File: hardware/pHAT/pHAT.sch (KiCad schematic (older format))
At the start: 16 parts, among them P1 Conn_02x20_Odd_Even, U2 HIH6131-021, U3 P82B96

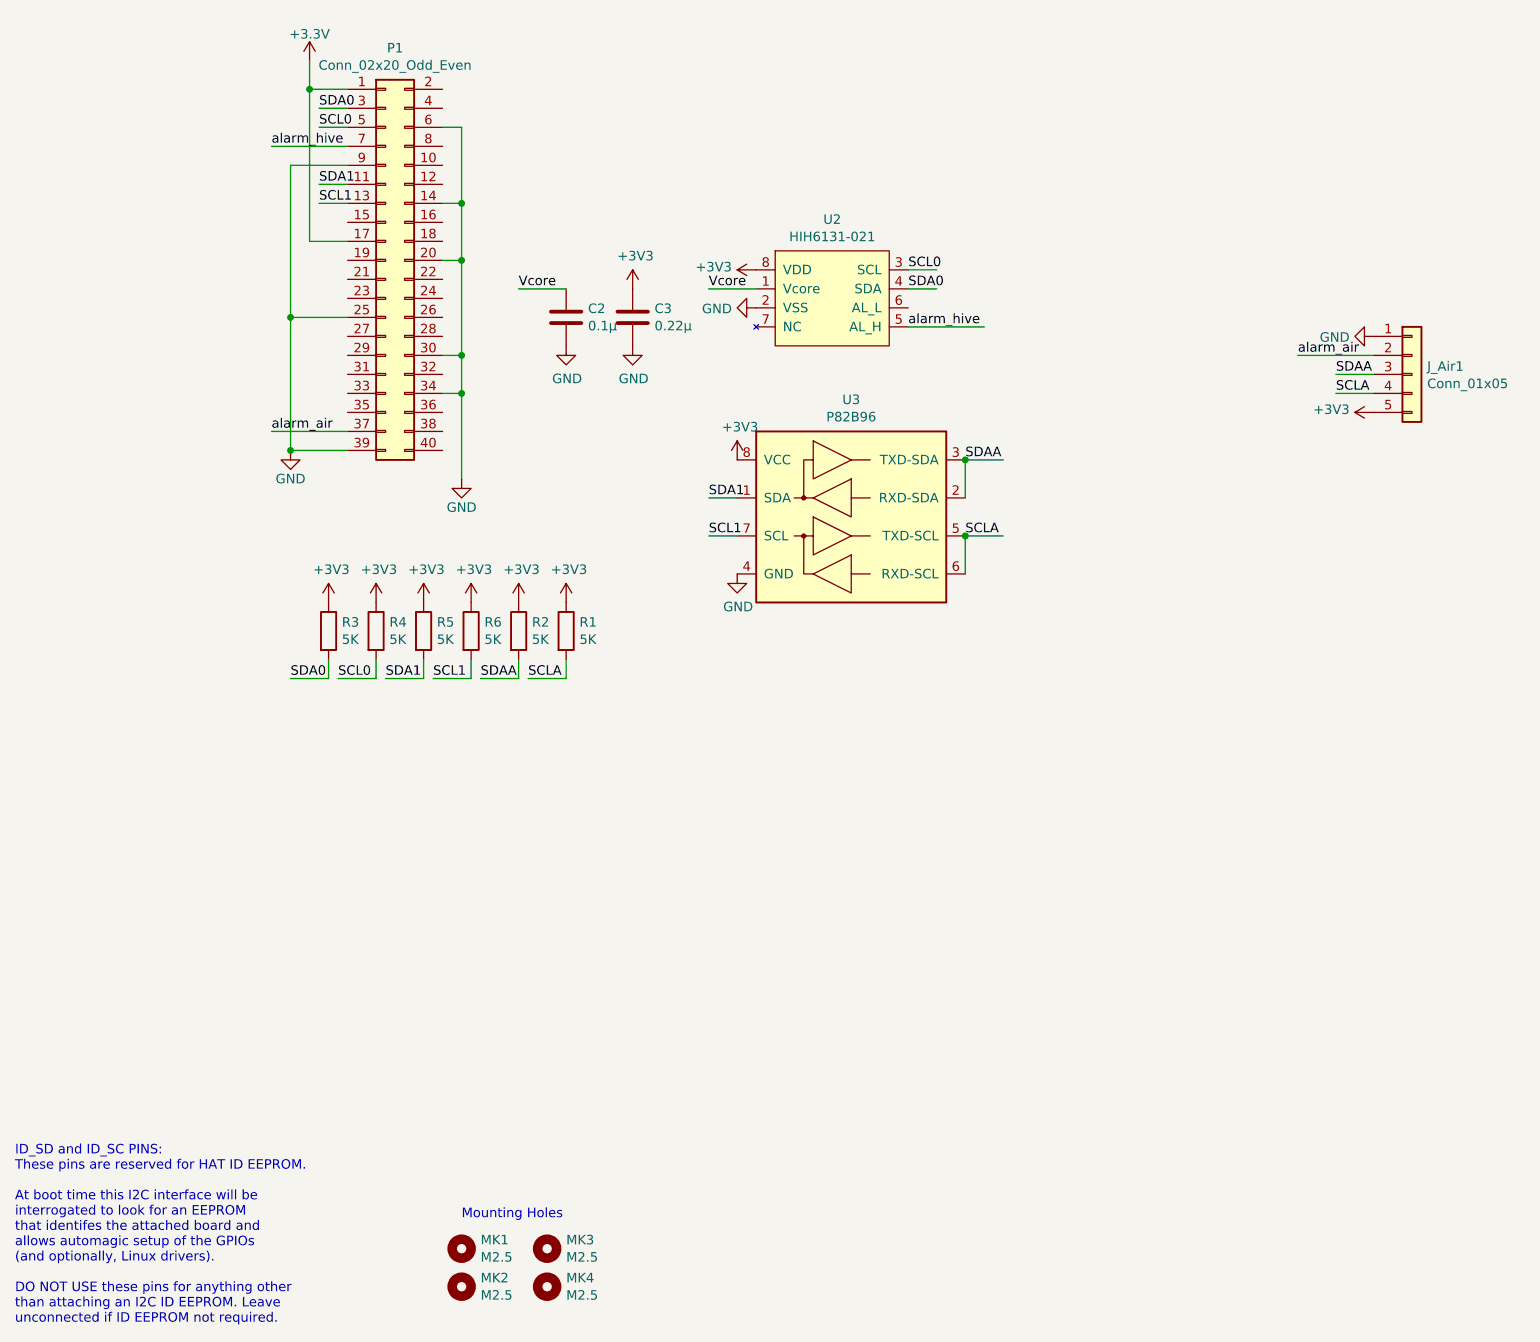
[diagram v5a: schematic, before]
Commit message: Preparing layout for adding a fan
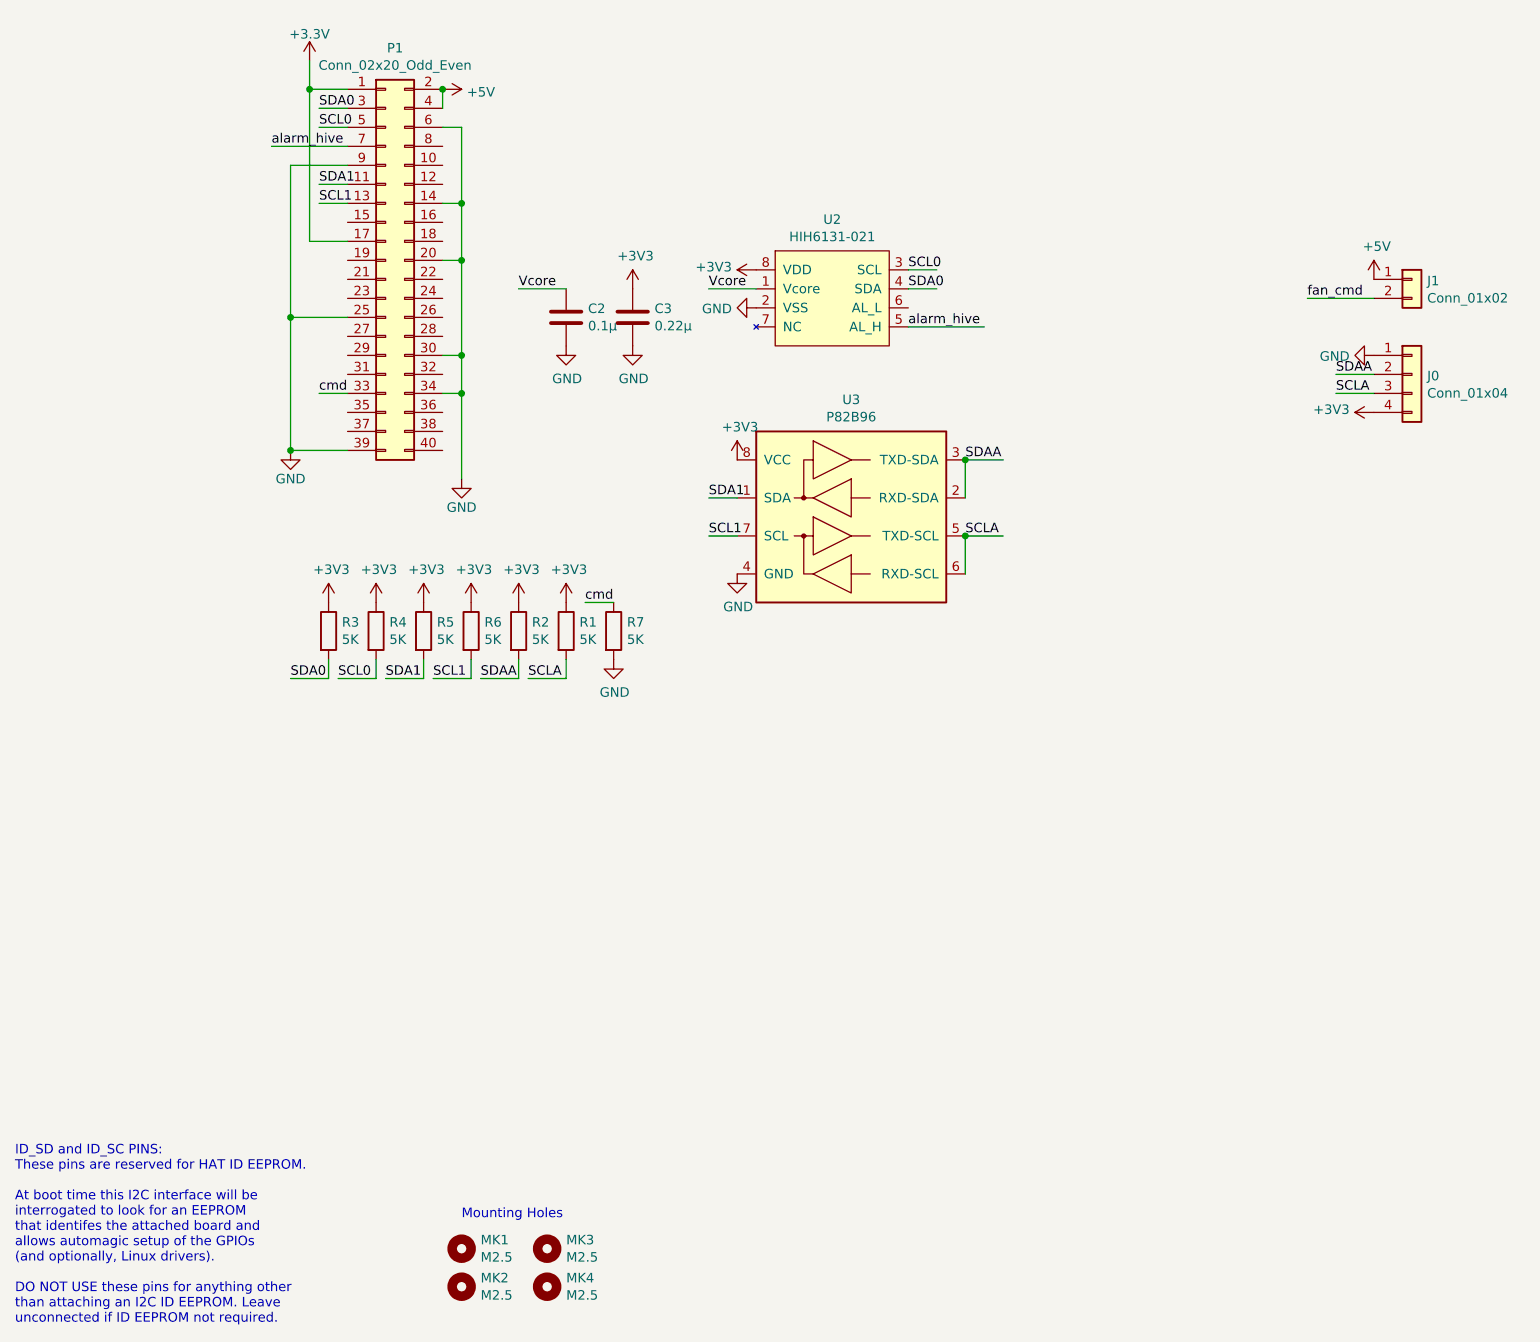
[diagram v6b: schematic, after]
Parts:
- removed J_Air1: Conn_01x05, Connector_Molex:Molex_KK-254_AE-6410-05A_1x05_P2.54mm_Vertical, symbol Connector_Generic:Conn_01x05
- added J0: Conn_01x04, Connector_Molex:Molex_KK-254_AE-6410-04A_1x04_P2.54mm_Vertical, symbol Connector_Generic:Conn_01x04
- added J1: Conn_01x02, Connector_Molex:Molex_KK-254_AE-6410-02A_1x02_P2.54mm_Vertical, symbol Connector_Generic:Conn_01x02
- added R7: 5K, Resistor_SMD:R_0805_2012Metric_Pad1.15x1.40mm_HandSolder, symbol Device:R
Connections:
- net labels added: +5V, cmd, fan_cmd
- net labels removed: alarm_air
- wire segments 51 -> 53
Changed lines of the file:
@@
 Sheet 1 1
 Title "Beehive pHAT"
-Date "2019-01-29"
-Rev "v2.1"
+Date "2019-02-13"
+Rev "v3.2"
 Comp "University of Glasgow"
 Comment1 ""
@@
 L power:GND #PWR0121
 U 1 1 5C4780F6
-P 7800 2400
-F 0 "#PWR0121" H 7800 2150 50  0001 C CNN
-F 1 "GND" V 7805 2272 50  0000 R CNN
-F 2 "" H 7800 2400 50  0001 C CNN
-F 3 "" H 7800 2400 50  0001 C CNN
-	1    7800 2400
+P 7800 2500
+F 0 "#PWR0121" H 7800 2250 50  0001 C CNN
+F 1 "GND" V 7805 2372 50  0000 R CNN
+F 2 "" H 7800 2500 50  0001 C CNN
+F 3 "" H 7800 2500 50  0001 C CNN
+	1    7800 2500
 	0    1    1    0
 $EndComp
@@
 	1    0    0    -1
 $EndComp
-$Comp
-L Connector_Generic:Conn_01x05 J_Air1
-U 1 1 5C50B707
-P 8000 2600
-F 0 "J_Air1" H 8080 2642 50  0000 L CNN
-F 1 "Conn_01x05" H 8080 2551 50  0000 L CNN
-F 2 "Connector_Molex:Molex_KK-254_AE-6410-05A_1x05_P2.54mm_Vertical" H 8000 2600 50  0001 C CNN
-F 3 "~" H 8000 2600 50  0001 C CNN
-	1    8000 2600
-	1    0    0    -1
-$EndComp
-Text Label 7400 2500 0    50   ~ 0
-alarm_air
-Wire Wire Line
-	7800 2500 7400 2500
 Text Label 2000 1400 0    50   ~ 0
 alarm_hive
 Wire Wire Line
 	2400 1400 2000 1400
-Text Label 2000 2900 0    50   ~ 0
-alarm_air
-Wire Wire Line
-	2400 2900 2000 2900
 $Comp
 L honeywell:HIHxx3x-021 U2
@@
 Wire Wire Line
 	3550 2150 3300 2150
+$Comp
+L Connector_Generic:Conn_01x04 J0
+U 1 1 5C646ECB
+P 8000 2600
+F 0 "J0" H 8080 2592 50  0000 L CNN
+F 1 "Conn_01x04" H 8080 2501 50  0000 L CNN
+F 2 "Connector_Molex:Molex_KK-254_AE-6410-04A_1x04_P2.54mm_Vertical" H 8000 2600 50  0001 C CNN
+F 3 "~" H 8000 2600 50  0001 C CNN
+	1    8000 2600
+	1    0    0    -1
+$EndComp
+$Comp
+L Connector_Generic:Conn_01x02 J1
+U 1 1 5C648B5C
+P 8000 2100
+F 0 "J1" H 8080 2092 50  0000 L CNN
+F 1 "Conn_01x02" H 8080 2001 50  0000 L CNN
+F 2 "Connector_Molex:Molex_KK-254_AE-6410-02A_1x02_P2.54mm_Vertical" H 8000 2100 50  0001 C CNN
+F 3 "~" H 8000 2100 50  0001 C CNN
+	1    8000 2100
+	1    0    0    -1
+$EndComp
+$Comp
+L power:+5V #PWR0101
+U 1 1 5C648C36
+P 7800 2100
+F 0 "#PWR0101" H 7800 1950 50  0001 C CNN
+F 1 "+5V" H 7815 2273 50  0000 C CNN
+F 2 "" H 7800 2100 50  0001 C CNN
+F 3 "" H 7800 2100 50  0001 C CNN
+	1    7800 2100
+	1    0    0    -1
+$EndComp
+$Comp
+L power:+5V #PWR0102
+U 1 1 5C648D8A
+P 2900 1100
+F 0 "#PWR0102" H 2900 950 50  0001 C CNN
+F 1 "+5V" V 2915 1228 50  0000 L CNN
+F 2 "" H 2900 1100 50  0001 C CNN
+F 3 "" H 2900 1100 50  0001 C CNN
+	1    2900 1100
+	0    1    1    0
+$EndComp
+Wire Wire Line
+	2900 1200 2900 1100
+Connection ~ 2900 1100
+Text Label 7450 2200 0    50   ~ 0
+fan_cmd
+Wire Wire Line
+	7800 2200 7450 2200
+Text Label 2250 2700 0    50   ~ 0
+cmd
+Wire Wire Line
+	2400 2700 2250 2700
+$Comp
+L Device:R R7
+U 1 1 5C66B531
+P 3800 3950
+F 0 "R7" H 3870 3996 50  0000 L CNN
+F 1 "5K" H 3870 3905 50  0000 L CNN
+F 2 "Resistor_SMD:R_0805_2012Metric_Pad1.15x1.40mm_HandSolder" V 3730 3950 50  0001 C CNN
+F 3 "~" H 3800 3950 50  0001 C CNN
+	1    3800 3950
+	1    0    0    -1
+$EndComp
+Text Label 3650 3800 0    50   ~ 0
+cmd
+Wire Wire Line
+	3800 3800 3650 3800
+$Comp
+L power:GND #PWR?
+U 1 1 5C6704A6
+P 3800 4100
+F 0 "#PWR?" H 3800 3850 50  0001 C CNN
+F 1 "GND" H 3805 3927 50  0000 C CNN
+F 2 "" H 3800 4100 50  0001 C CNN
+F 3 "" H 3800 4100 50  0001 C CNN
+	1    3800 4100
+	1    0    0    -1
+$EndComp
 $EndSCHEMATC

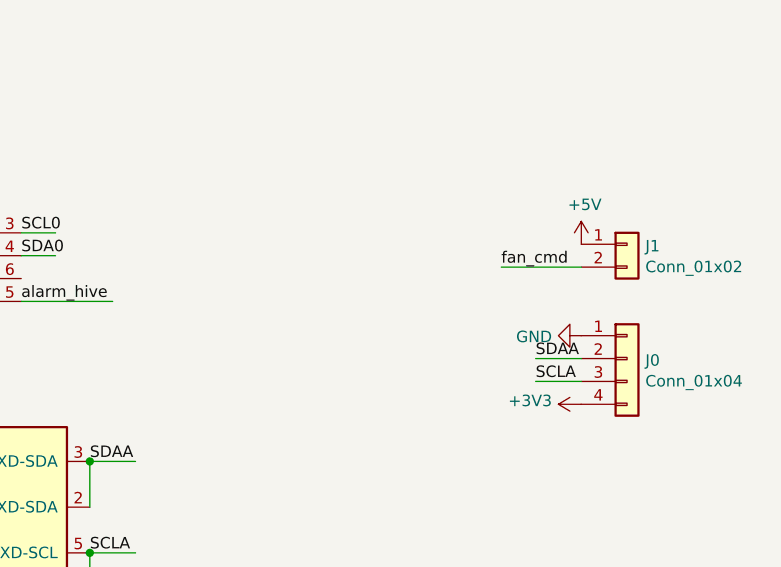
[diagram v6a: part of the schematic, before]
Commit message: Finished fan command circuit (pHAT v3.2)
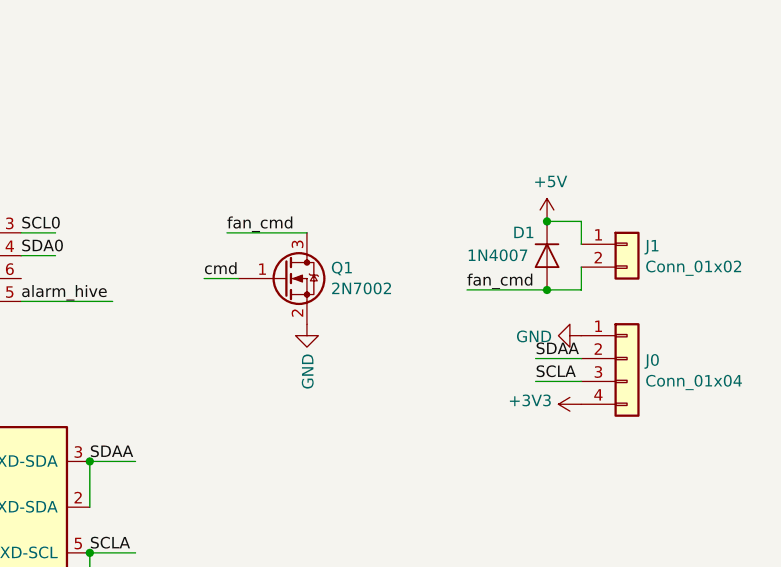
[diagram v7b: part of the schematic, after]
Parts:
- added D1: 1N4007, Diode_THT:D_DO-41_SOD81_P10.16mm_Horizontal, symbol Diode:1N4007
- added Q1: 2N7002, Package_TO_SOT_SMD:SOT-23, symbol Transistor_FET:2N7002
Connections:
- wire segments 53 -> 59
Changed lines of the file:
@@
 Sheet 1 1
 Title "Beehive pHAT"
-Date "2019-02-13"
+Date "2019-02-18"
 Rev "v3.2"
 Comp "University of Glasgow"
@@
 L power:+5V #PWR0101
 U 1 1 5C648C36
-P 7800 2100
-F 0 "#PWR0101" H 7800 1950 50  0001 C CNN
-F 1 "+5V" H 7815 2273 50  0000 C CNN
-F 2 "" H 7800 2100 50  0001 C CNN
-F 3 "" H 7800 2100 50  0001 C CNN
-	1    7800 2100
+P 7650 2000
+F 0 "#PWR0101" H 7650 1850 50  0001 C CNN
+F 1 "+5V" H 7665 2173 50  0000 C CNN
+F 2 "" H 7650 2000 50  0001 C CNN
+F 3 "" H 7650 2000 50  0001 C CNN
+	1    7650 2000
 	1    0    0    -1
 $EndComp
@@
 	2900 1200 2900 1100
 Connection ~ 2900 1100
-Text Label 7450 2200 0    50   ~ 0
+Text Label 7300 2300 0    50   ~ 0
 fan_cmd
 Wire Wire Line
-	7800 2200 7450 2200
+	7650 2300 7300 2300
 Text Label 2250 2700 0    50   ~ 0
 cmd
@@
 	3800 3800 3650 3800
 $Comp
-L power:GND #PWR?
+L power:GND #PWR0103
 U 1 1 5C6704A6
 P 3800 4100
-F 0 "#PWR?" H 3800 3850 50  0001 C CNN
+F 0 "#PWR0103" H 3800 3850 50  0001 C CNN
 F 1 "GND" H 3805 3927 50  0000 C CNN
 F 2 "" H 3800 4100 50  0001 C CNN
@@
 	1    0    0    -1
 $EndComp
+$Comp
+L Transistor_FET:2N7002 Q1
+U 1 1 5C6AACFD
+P 6500 2250
+F 0 "Q1" H 6705 2296 50  0000 L CNN
+F 1 "2N7002" H 6705 2205 50  0000 L CNN
+F 2 "Package_TO_SOT_SMD:SOT-23" H 6700 2175 50  0001 L CIN
+F 3 "https://www.fairchildsemi.com/datasheets/2N/2N7002.pdf" H 6500 2250 50  0001 L CNN
+	1    6500 2250
+	1    0    0    -1
+$EndComp
+Text Label 6150 2250 0    50   ~ 0
+cmd
+Wire Wire Line
+	6300 2250 6150 2250
+$Comp
+L power:GND #PWR0105
+U 1 1 5C6ABD61
+P 6600 2450
+F 0 "#PWR0105" H 6600 2200 50  0001 C CNN
+F 1 "GND" V 6605 2322 50  0000 R CNN
+F 2 "" H 6600 2450 50  0001 C CNN
+F 3 "" H 6600 2450 50  0001 C CNN
+	1    6600 2450
+	1    0    0    -1
+$EndComp
+Text Label 6250 2050 0    50   ~ 0
+fan_cmd
+Wire Wire Line
+	6600 2050 6250 2050
+$Comp
+L Diode:1N4007 D1
+U 1 1 5C6AF374
+P 7650 2150
+F 0 "D1" V 7550 2000 50  0000 L CNN
+F 1 "1N4007" V 7650 1800 50  0000 L CNN
+F 2 "Diode_THT:D_DO-41_SOD81_P10.16mm_Horizontal" H 7650 1975 50  0001 C CNN
+F 3 "http://www.vishay.com/docs/88503/1n4001.pdf" H 7650 2150 50  0001 C CNN
+	1    7650 2150
+	0    1    1    0
+$EndComp
+Wire Wire Line
+	7800 2000 7650 2000
+Wire Wire Line
+	7800 2000 7800 2100
+Connection ~ 7650 2000
+Wire Wire Line
+	7800 2200 7800 2300
+Wire Wire Line
+	7800 2300 7650 2300
+Connection ~ 7650 2300
 $EndSCHEMATC

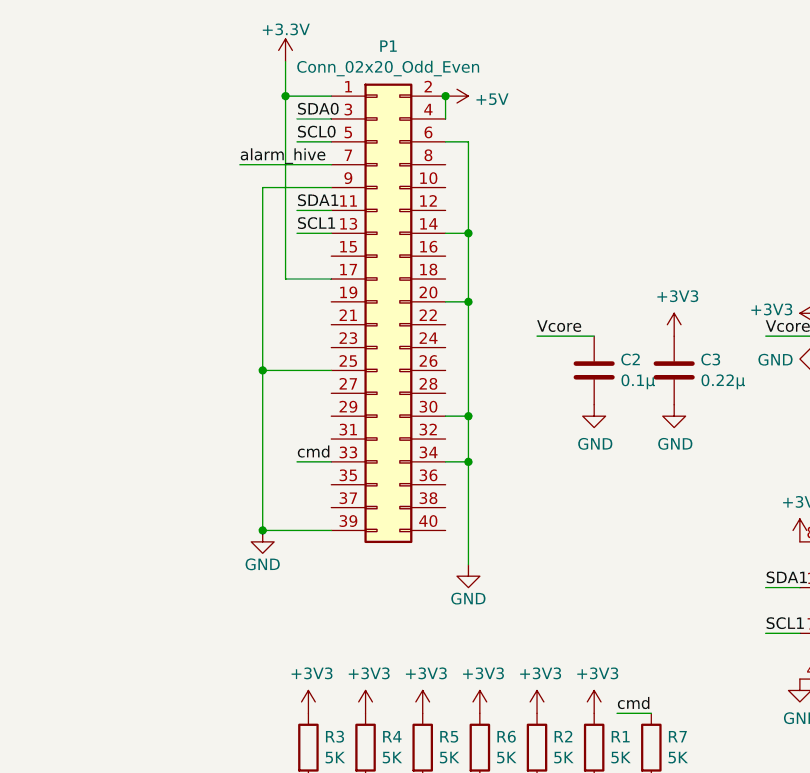
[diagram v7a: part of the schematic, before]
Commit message: Rework of sensor board and correction of pHAT
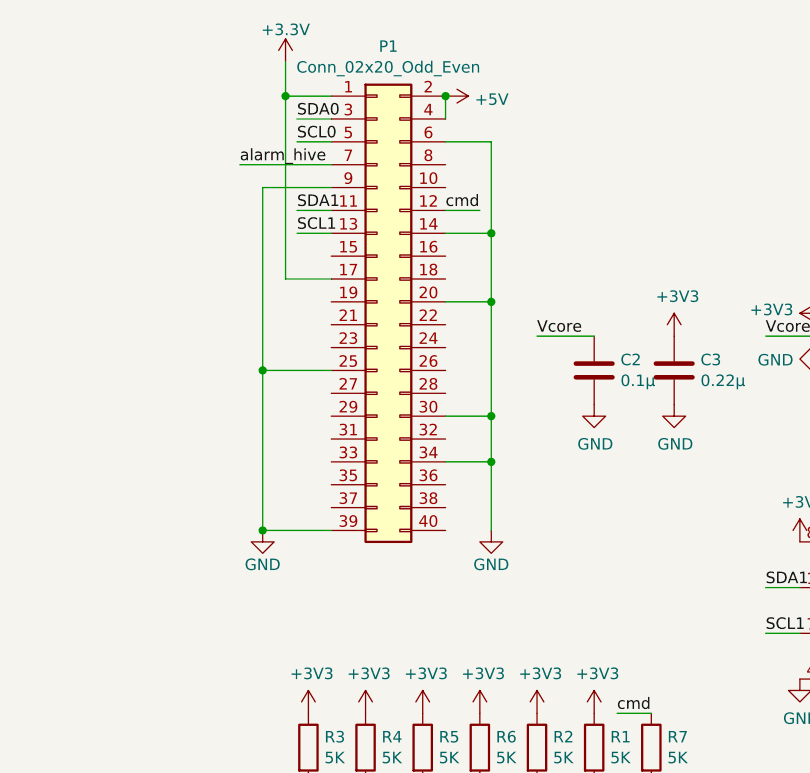
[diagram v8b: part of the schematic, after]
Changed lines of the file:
@@
 Sheet 1 1
 Title "Beehive pHAT"
-Date "2019-02-18"
-Rev "v3.2"
+Date "2019-03-12"
+Rev "v3.3"
 Comp "University of Glasgow"
 Comment1 ""
@@
 L power:GND #PWR02
 U 1 1 580C1D11
-P 3000 3150
-F 0 "#PWR02" H 3000 2900 50  0001 C CNN
-F 1 "GND" H 3000 3000 50  0000 C CNN
-F 2 "" H 3000 3150 50  0000 C CNN
-F 3 "" H 3000 3150 50  0000 C CNN
-	1    3000 3150
-	1    0    0    -1
-$EndComp
-Wire Wire Line
-	3000 1300 3000 1700
-Wire Wire Line
-	3000 2700 2900 2700
-Wire Wire Line
-	3000 2500 2900 2500
-Connection ~ 3000 2700
-Wire Wire Line
-	3000 2000 2900 2000
-Connection ~ 3000 2500
-Wire Wire Line
-	3000 1700 2900 1700
-Connection ~ 3000 2000
+P 3100 3000
+F 0 "#PWR02" H 3100 2750 50  0001 C CNN
+F 1 "GND" H 3100 2850 50  0000 C CNN
+F 2 "" H 3100 3000 50  0000 C CNN
+F 3 "" H 3100 3000 50  0000 C CNN
+	1    3100 3000
+	1    0    0    -1
+$EndComp
+Wire Wire Line
+	3100 1300 3100 1700
+Wire Wire Line
+	3100 2700 2900 2700
+Wire Wire Line
+	3100 2500 2900 2500
+Connection ~ 3100 2700
+Wire Wire Line
+	3100 2000 2900 2000
+Connection ~ 3100 2500
+Wire Wire Line
+	3100 1700 2900 1700
+Connection ~ 3100 2000
 $Comp
 L power:GND #PWR03
@@
 SCL0
 Wire Wire Line
-	3000 1300 2900 1300
-Connection ~ 3000 1700
+	3100 1300 2900 1300
+Connection ~ 3100 1700
 Text Notes 650  7600 0    50   ~ 0
 ID_SD and ID_SC PINS:\nThese pins are reserved for HAT ID EEPROM.\n\nAt boot time this I2C interface will be\ninterrogated to look for an EEPROM\nthat identifes the attached board and\nallows automagic setup of the GPIOs\n(and optionally, Linux drivers).\n\nDO NOT USE these pins for anything other\nthan attaching an I2C ID EEPROM. Leave\nunconnected if ID EEPROM not required.
@@
 $EndComp
 Wire Wire Line
-	3000 2700 3000 3150
-Wire Wire Line
-	3000 2500 3000 2700
-Wire Wire Line
-	3000 2000 3000 2500
+	3100 2700 3100 3000
+Wire Wire Line
+	3100 2500 3100 2700
+Wire Wire Line
+	3100 2000 3100 2500
 Wire Wire Line
 	2200 1100 2200 1900
@@
 	2100 2300 2100 3000
 Wire Wire Line
-	3000 1700 3000 2000
+	3100 1700 3100 2000
 $Comp
 L Device:R R3
@@
 Wire Wire Line
 	7650 2300 7300 2300
-Text Label 2250 2700 0    50   ~ 0
+Text Label 2900 1600 0    50   ~ 0
 cmd
 Wire Wire Line
-	2400 2700 2250 2700
+	3050 1600 2900 1600
 $Comp
 L Device:R R7
